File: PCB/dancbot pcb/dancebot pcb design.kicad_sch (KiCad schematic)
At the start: 26 parts, among them J1 ESP32-PICO-KIT-V4.1, J2 Voltage Regulator, J4 Pins, J6 Conn_01x04_Socket, J7 Conn_01x04_Socket, Q1 PMOS, Q2 PMOS, Q3 2N3904, Q5 PMOS, SW1 SP switch, SW2 SW_SPST

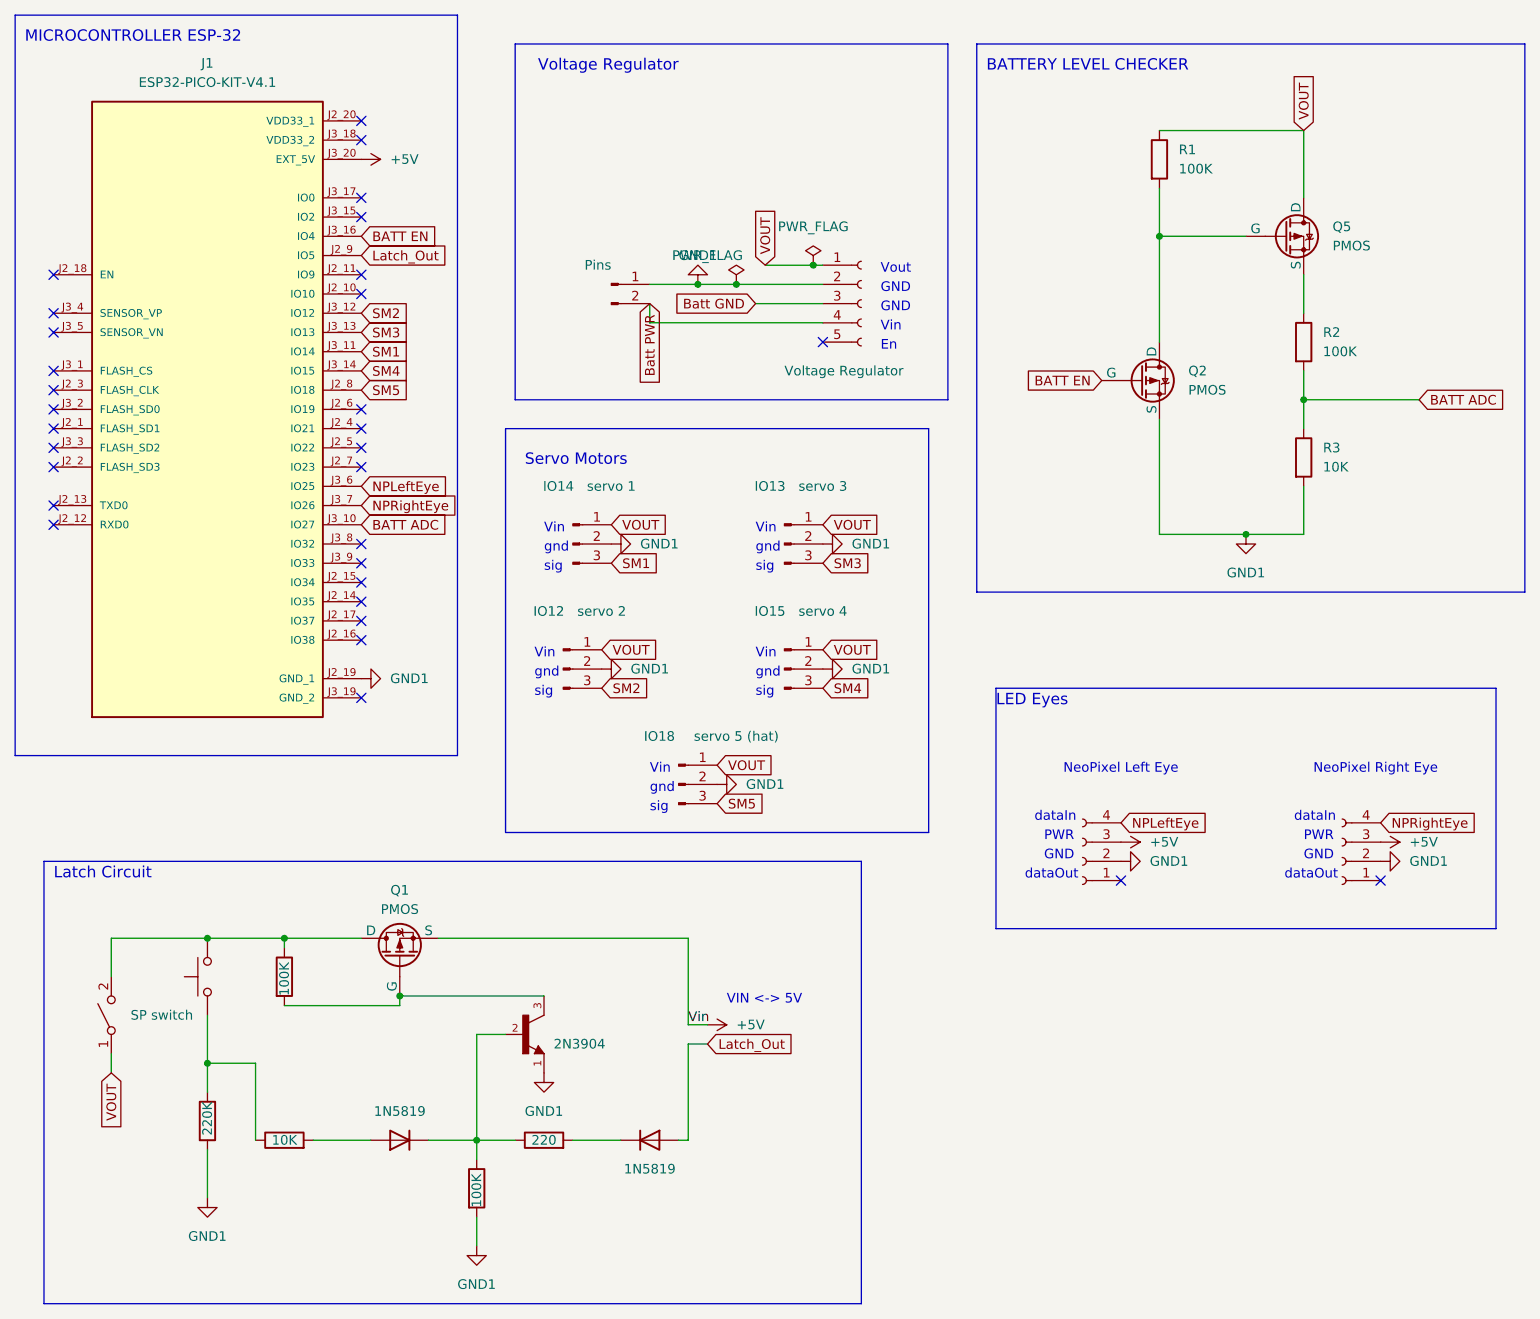
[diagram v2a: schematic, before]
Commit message: Routing rev 6, trace width increased, smd components added
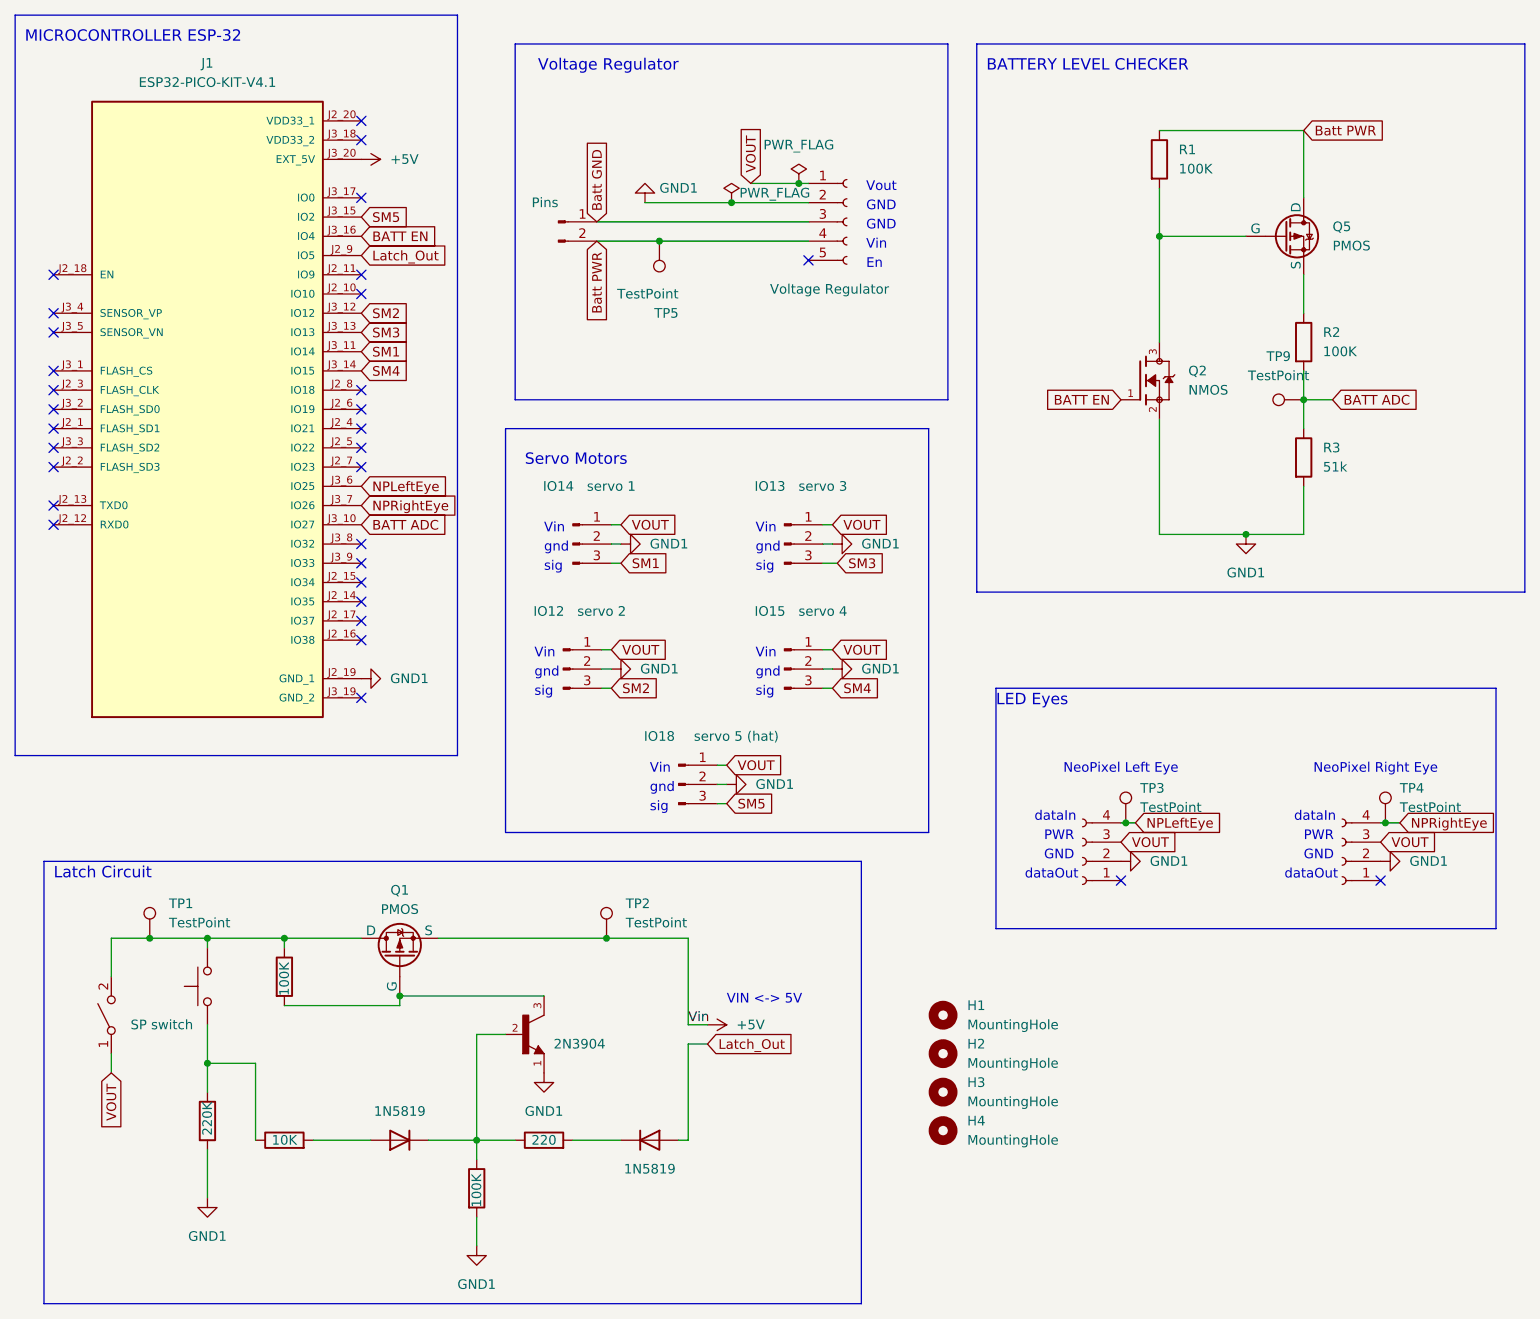
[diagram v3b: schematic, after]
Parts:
- added H1, H2, H3, H4: MountingHole, MountingHole:MountingHole_3.2mm_M3, symbol Mechanical:MountingHole
- added TP1, TP2, TP3, TP4, TP5, TP9: TestPoint, TestPoint:TestPoint_Pad_2.0x2.0mm, symbol Connector:TestPoint
- IO12, IO13, IO14, IO15, IO18: footprint Connector_PinHeader_1.00mm:PinHeader_1x03_P1.00mm_Vertical -> Connector_PinHeader_2.54mm:PinHeader_1x03_P2.54mm_Vertical
- J2: footprint Connector_PinSocket_1.00mm:PinSocket_1x05_P1.00mm_Vertical -> Connector_PinSocket_2.54mm:PinSocket_1x05_P2.54mm_Vertical
- J4, SW1, SW2: footprint Connector_PinHeader_1.00mm:PinHeader_1x02_P1.00mm_Vertical -> Connector_PinHeader_2.54mm:PinHeader_1x02_P2.54mm_Vertical
- J6, J7: footprint Connector_PinSocket_1.00mm:PinSocket_1x04_P1.00mm_Vertical -> Connector_PinSocket_2.54mm:PinSocket_1x04_P2.54mm_Vertical
- Q2: value PMOS -> NMOS; footprint dancebot pcb libraries stuff:TO254P1052X465X1989-3 -> Dancebot Footprints:SOT95P237X112-3N; symbol Simulation_SPICE:PMOS -> IRML2502:IRLML2502; Availability (none) -> In Stock; Check_prices (none) -> https://www.snapeda.com/parts/IRLML2502/Infineon+Technologi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; MANUFACTURER (none) -> Infineon Technologies; MAXIMUM_PACKAGE_HEIGHT (none) -> 1.12 mm; MF (none) -> Infineon Technologies; MP (none) -> IRLML2502; PARTREV (none) -> April 24, 2014; Package (none) -> SOT-23-3 International Rectifier; Price (none) -> None; Purchase-URL (none) -> https://www.snapeda.com/api/url_track_click_mouser/?unipart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; SNAPEDA_PACKAGE_ID (none) -> 11907; SNAPEDA_PN (none) -> IRLML2502; STANDARD (none) -> IPC 7351B; SnapEDA_Link (none) -> https://www.snapeda.com/parts/IRLML2502/Infineon+Technologi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
- Q5: footprint dancebot pcb libraries stuff:TO254P1052X465X1989-3 -> Dancebot Footprints:TO254P1052X465X1989-3
- R3: value 10K -> 51k
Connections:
- net +5V: now also TP2.1; no longer J6.3 (Pin_3), J7.3 (Pin_3)
- net BATT ADC: now also TP9.1
- net BATT EN: now also Q2.1; no longer Q2.2 (G)
- net Batt GND: now also J4.1 (Pin_1)
- net Batt PWR: now also Q5.1 (D), R1.1, TP5.1
- net GND1: now also Q2.2; no longer J4.1 (Pin_1), Q2.3 (S)
- net NPLeftEye: now also TP3.1
- net NPRightEye: now also TP4.1
- net SM5: now also J1.J3_15 (IO2); no longer J1.J2_8 (IO18)
- net VOUT: now also J6.3 (Pin_3), J7.3 (Pin_3); no longer Q5.1 (D), R1.1
- net at Q1.1 (D), R5.1, SW1.2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: now also TP1.1
- net at Q5.2 (G), R1.2: now also Q2.3; no longer Q2.1 (D)

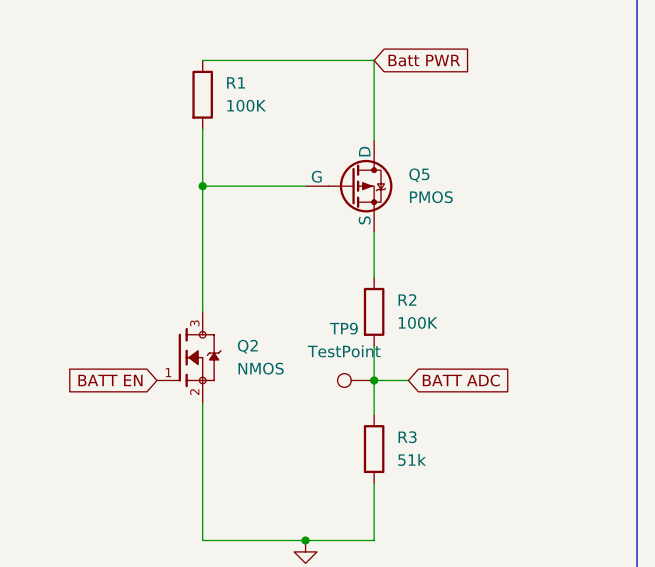
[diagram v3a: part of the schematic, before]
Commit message: Routing rev6, swapped MOSFETs THT w/ SMD, fixed some clearence issues
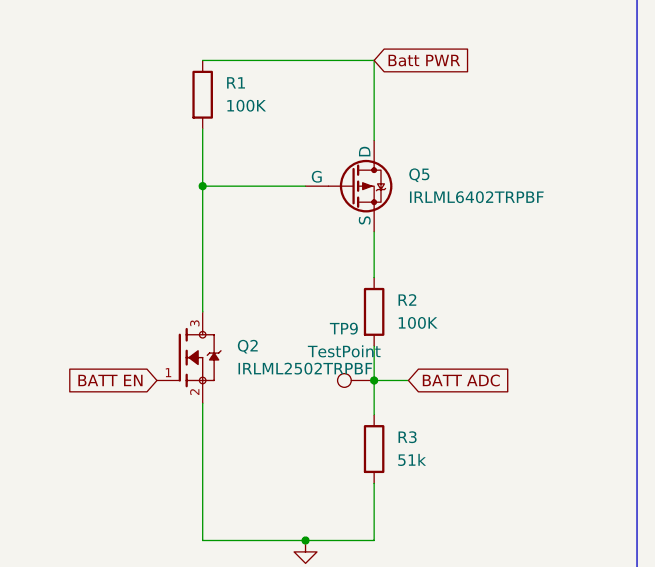
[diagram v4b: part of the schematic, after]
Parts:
- Q1: footprint dancebot pcb libraries stuff:TO254P1052X465X1989-3 -> Dancebot Footprints:SQ2351CES
- Q2: value NMOS -> IRLML2502TRPBF
- Q3: footprint 2N3904:TO92127P495H495-3 -> Dancebot Footprints:2N3904TFR
- Q5: value PMOS -> IRLML6402TRPBF; footprint Dancebot Footprints:TO254P1052X465X1989-3 -> Dancebot Footprints:IRLML6402TRPBF
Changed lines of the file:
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@@
       (effects (font (size 1.27 1.27)))
     )
-    (property "Footprint" "dancebot pcb libraries stuff:TO254P1052X465X1989-3" (at 64.77 134.62 0)
+    (property "Footprint" "Dancebot Footprints:SQ2351CES" (at 64.77 134.62 0)
       (effects (font (size 1.27 1.27)) hide)
     )
@@
       (effects (font (size 1.27 1.27)) (justify left))
     )
-    (property "Value" "NMOS" (at 171.45 64.77 0)
+    (property "Value" "IRLML2502TRPBF" (at 171.45 64.77 0)
       (effects (font (size 1.27 1.27)) (justify left))
     )
@@
       (effects (font (size 1.27 1.27)) (justify left))
     )
-    (property "Value" "PMOS" (at 190.5 45.72 0)
-      (effects (font (size 1.27 1.27)) (justify left))
-    )
-    (property "Footprint" "Dancebot Footprints:TO254P1052X465X1989-3" (at 189.23 41.91 0)
+    (property "Value" "IRLML6402TRPBF" (at 190.5 45.72 0)
+      (effects (font (size 1.27 1.27)) (justify left))
+    )
+    (property "Footprint" "Dancebot Footprints:IRLML6402TRPBF" (at 189.23 41.91 0)
       (effects (font (size 1.27 1.27)) hide)
     )
@@
       (effects (font (size 1.27 1.27)) (justify left))
     )
-    (property "Footprint" "2N3904:TO92127P495H495-3" (at 83.82 149.86 0)
-      (effects (font (size 1.27 1.27)) (justify bottom) hide)
-    )
+    (property "Footprint" "Dancebot Footprints:2N3904TFR" (at 83.82 149.86 0)
+      (effects (font (size 1.27 1.27)) (justify bottom) hide)
+    )
